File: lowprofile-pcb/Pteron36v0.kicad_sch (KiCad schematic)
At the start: 47 parts, among them J1 AudioJack4, J2 AudioJack4, SW1 SW_PUSH, SW10 SW_PUSH, SW12 SW_PUSH, SW13 SW_PUSH, SW14 SW_PUSH, SW15 SW_PUSH, SW17 SW_PUSH, SW18 SW_PUSH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

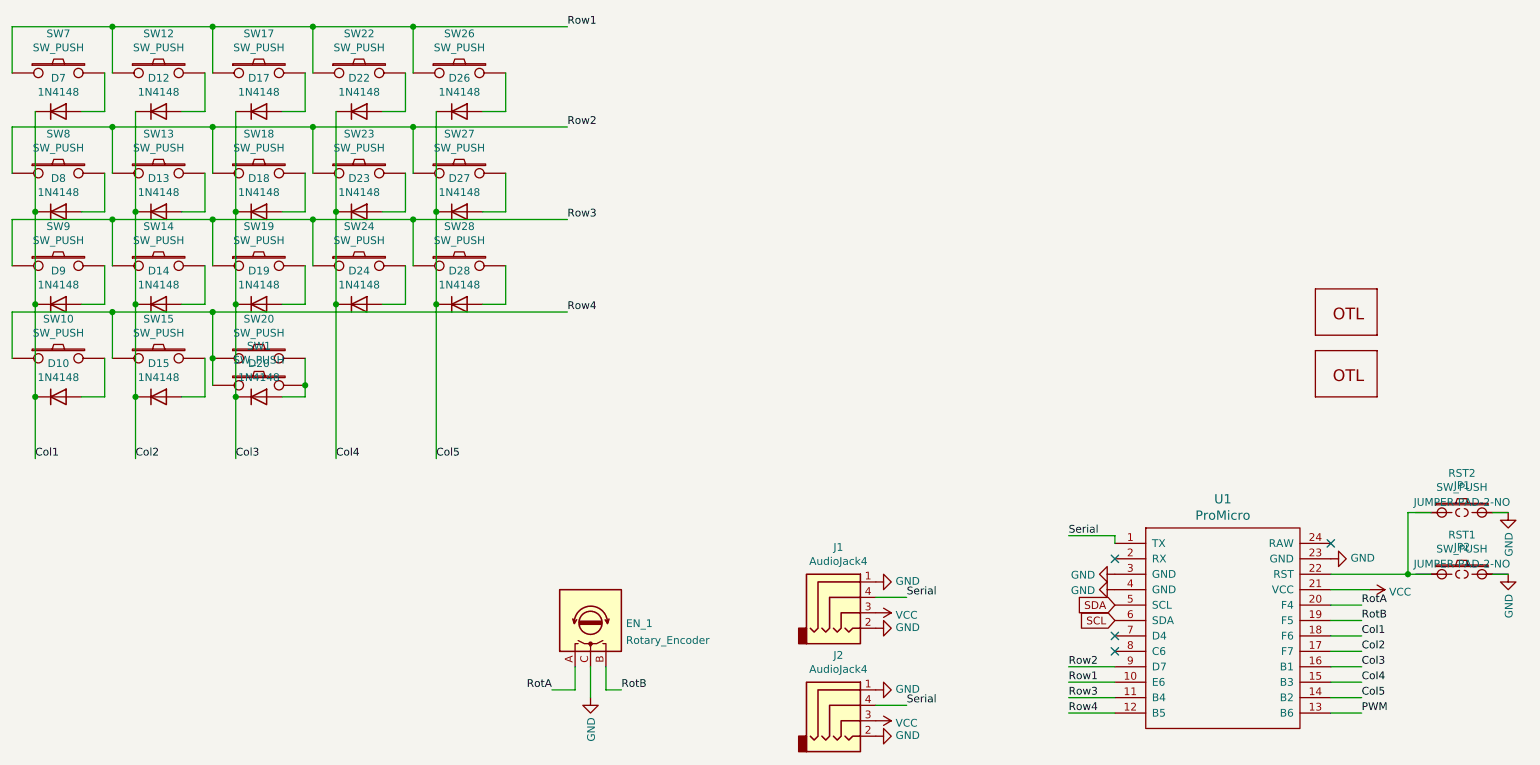
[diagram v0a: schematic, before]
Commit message: add 4-th key in thumb for removable config
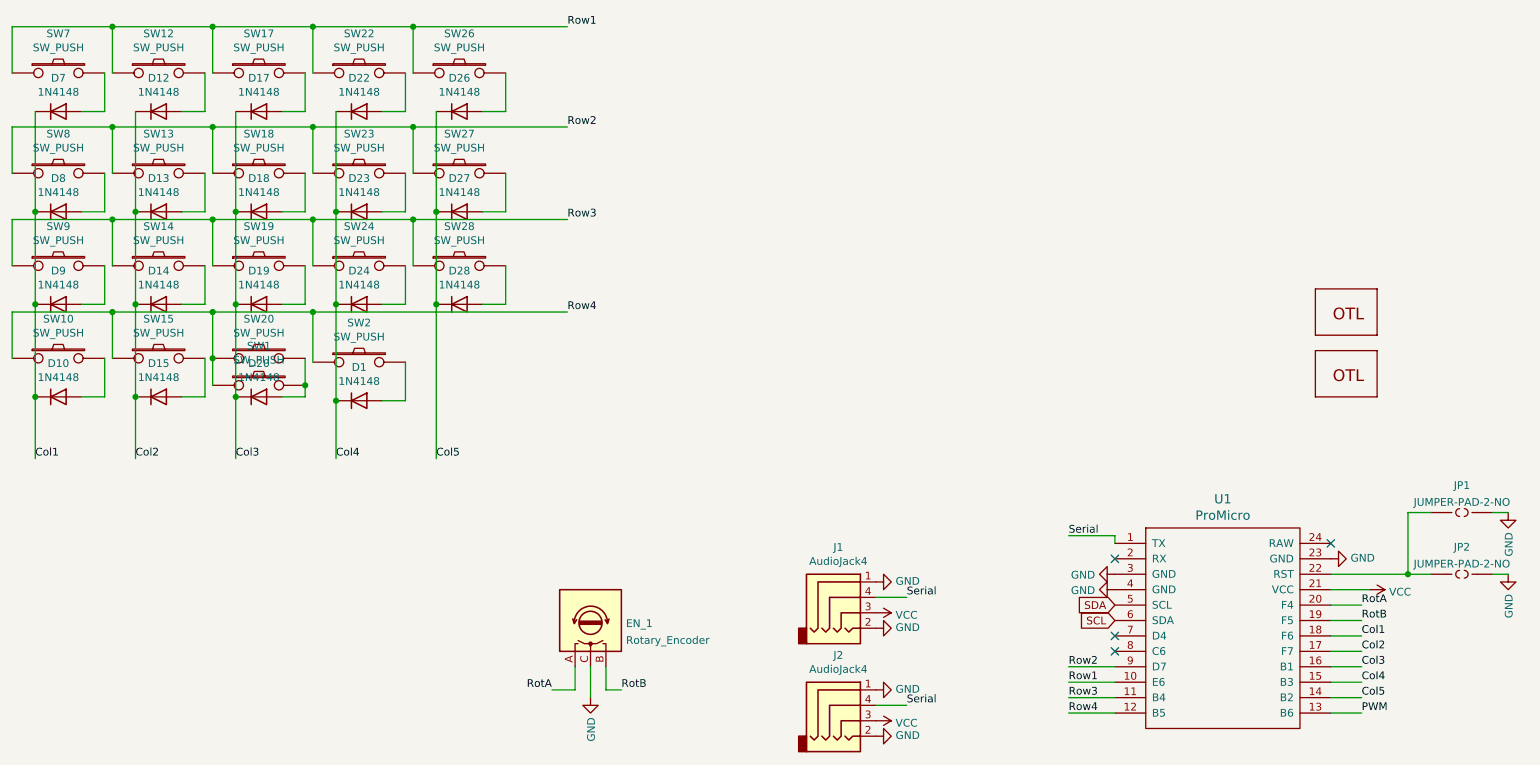
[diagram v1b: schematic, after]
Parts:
- removed RST1, RST2: SW_PUSH, acheron_Hardware:smdPushBtn, symbol keyboard_parts:SW_PUSH
- added D1: 1N4148, Keebio-Parts:Diode-dual, symbol Diode:1N4148
- added SW2: SW_PUSH, keyswitches:PG1350_reversible, symbol keyboard_parts:SW_PUSH
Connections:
- net Col4: now also D1.1 (K)
- net Row4: now also SW2.1
- new net: D1.2 (A), SW2.2
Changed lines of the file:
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@@
   (junction (at 81.28 46.99) (diameter 1.016) (color 0 0 0 0))
   (junction (at 81.28 62.23) (diameter 1.016) (color 0 0 0 0))
+  (junction (at 81.28 77.47) (diameter 1.016) (color 0 0 0 0))
   (junction (at 85.09 60.96) (diameter 1.016) (color 0 0 0 0))
   (junction (at 85.09 76.2) (diameter 1.016) (color 0 0 0 0))
+  (junction (at 85.09 92.075) (diameter 1.016) (color 0 0 0 0))
   (junction (at 97.79 30.48) (diameter 1.016) (color 0 0 0 0))
   (junction (at 97.79 46.99) (diameter 1.016) (color 0 0 0 0))
@@
     (stroke (width 0) (type solid) (color 0 0 0 0))
   )
-  (wire (pts (xy 64.77 77.47) (xy 123.19 77.47))
+  (wire (pts (xy 64.77 77.47) (xy 81.28 77.47))
     (stroke (width 0) (type solid) (color 0 0 0 0))
   )
@@
     (stroke (width 0) (type solid) (color 0 0 0 0))
   )
+  (wire (pts (xy 81.28 77.47) (xy 81.28 85.725))
+    (stroke (width 0) (type solid) (color 0 0 0 0))
+  )
+  (wire (pts (xy 81.28 77.47) (xy 123.19 77.47))
+    (stroke (width 0) (type solid) (color 0 0 0 0))
+  )
   (wire (pts (xy 85.09 60.96) (xy 85.09 44.45))
     (stroke (width 0) (type solid) (color 0 0 0 0))
@@
     (stroke (width 0) (type solid) (color 0 0 0 0))
   )
-  (wire (pts (xy 85.09 76.2) (xy 85.09 101.6))
+  (wire (pts (xy 85.09 76.2) (xy 85.09 92.075))
+    (stroke (width 0) (type solid) (color 0 0 0 0))
+  )
+  (wire (pts (xy 85.09 92.075) (xy 85.09 101.6))
     (stroke (width 0) (type solid) (color 0 0 0 0))
   )
@@
   )
   (wire (pts (xy 96.52 76.2) (xy 92.71 76.2))
+    (stroke (width 0) (type solid) (color 0 0 0 0))
+  )
+  (wire (pts (xy 96.52 85.725) (xy 96.52 92.075))
+    (stroke (width 0) (type solid) (color 0 0 0 0))
+  )
+  (wire (pts (xy 96.52 92.075) (xy 92.71 92.075))
     (stroke (width 0) (type solid) (color 0 0 0 0))
   )
@@
     (pin "2")
   )
+  (symbol (lib_id "Diode:1N4148") (at 88.9 92.075 0) (unit 1)
+    (in_bom yes) (on_board yes)
+    (property "Reference" "D1" (id 0) (at 88.9 86.5632 0))
+    (property "Value" "1N4148" (id 1) (at 88.9 88.8746 0))
+    (property "Footprint" "Keebio-Parts:Diode-dual" (id 2) (at 88.9 96.52 0)
+      (effects (font (size 1.27 1.27)) hide)
+    )
+    (property "Datasheet" "https://assets.nexperia.com/documents/data-sheet/1N4148_1N4448.pdf" (id 3) (at 88.9 92.075 0)
+      (effects (font (size 1.27 1.27)) hide)
+    )
+    (pin "1")
+    (pin "2")
+  )
   (symbol (lib_id "Diode:1N4148") (at 105.41 44.45 0) (unit 1)
     (in_bom yes) (on_board yes)
@@
     (pin "2")
   )
+  (symbol (lib_id "keyboard_parts:SW_PUSH") (at 88.9 85.725 0) (unit 1)
+    (in_bom yes) (on_board yes)
+    (property "Reference" "SW2" (id 0) (at 88.9 79.248 0))
+    (property "Value" "SW_PUSH" (id 1) (at 88.9 81.5594 0))
+    (property "Footprint" "keyswitches:PG1350_reversible" (id 2) (at 88.9 85.725 0)
+      (effects (font (size 1.524 1.524)) hide)
+    )
+    (property "Datasheet" "" (id 3) (at 88.9 85.725 0)
+      (effects (font (size 1.524 1.524)))
+    )
+    (pin "1")
+    (pin "2")
+  )
   (symbol (lib_id "keyboard_parts:SW_PUSH") (at 105.41 38.1 0) (unit 1)
     (in_bom yes) (on_board yes)
@@
     )
     (property "Datasheet" "" (id 3) (at 105.41 69.85 0)
-      (effects (font (size 1.524 1.524)))
-    )
-    (pin "1")
-    (pin "2")
-  )
-  (symbol (lib_id "keyboard_parts:SW_PUSH") (at 270.51 110.49 0) (unit 1)
-    (in_bom yes) (on_board yes)
-    (property "Reference" "RST2" (id 0) (at 270.51 104.013 0))
-    (property "Value" "SW_PUSH" (id 1) (at 270.51 106.3244 0))
-    (property "Footprint" "acheron_Hardware:smdPushBtn" (id 2) (at 270.51 110.49 0)
-      (effects (font (size 1.524 1.524)) hide)
-    )
-    (property "Datasheet" "" (id 3) (at 270.51 110.49 0)
-      (effects (font (size 1.524 1.524)))
-    )
-    (pin "1")
-    (pin "2")
-  )
-  (symbol (lib_id "keyboard_parts:SW_PUSH") (at 270.51 120.65 0) (unit 1)
-    (in_bom yes) (on_board yes)
-    (property "Reference" "RST1" (id 0) (at 270.51 114.173 0))
-    (property "Value" "SW_PUSH" (id 1) (at 270.51 116.4844 0))
-    (property "Footprint" "acheron_Hardware:smdPushBtn" (id 2) (at 270.51 120.65 0)
-      (effects (font (size 1.524 1.524)) hide)
-    )
-    (property "Datasheet" "" (id 3) (at 270.51 120.65 0)
       (effects (font (size 1.524 1.524)))
     )
@@
       (reference "#PWR0118") (unit 1) (value "GND") (footprint "")
     )
+    (path "/703bd629-2fdb-4790-be4c-4af2160ffc24"
+      (reference "D1") (unit 1) (value "1N4148") (footprint "Keebio-Parts:Diode-dual")
+    )
     (path "/00000000-0000-0000-0000-000060962387"
       (reference "D7") (unit 1) (value "1N4148") (footprint "Keebio-Parts:Diode-dual")
@@
       (reference "J2") (unit 1) (value "AudioJack4") (footprint "Keebio-Parts:TRRS-PJ-320A")
     )
+    (path "/0b76a048-da1d-4d10-82af-9264c0605235"
+      (reference "JP1") (unit 1) (value "JUMPER-PAD-2-NO") (footprint "Jumper:SolderJumper-2_P1.3mm_Open_Pad1.0x1.5mm")
+    )
+    (path "/c097909c-92c1-4c73-bddc-504d7eb669e6"
+      (reference "JP2") (unit 1) (value "JUMPER-PAD-2-NO") (footprint "Jumper:SolderJumper-2_P1.3mm_Open_Pad1.0x1.5mm")
+    )
     (path "/e4d4d865-3cb1-431d-b18c-3cc2928a93c9"
       (reference "LOGO3") (unit 1) (value "LOGO-OTL") (footprint "personal-logo:peacock-medium")
@@
       (reference "LOGO4") (unit 1) (value "LOGO-OTL") (footprint "personal-logo:peacock-medium")
     )
-    (path "/00000000-0000-0000-0000-0000607b81a2"
-      (reference "RST1") (unit 1) (value "SW_PUSH") (footprint "acheron_Hardware:smdPushBtn")
-    )
-    (path "/00000000-0000-0000-0000-0000607e0b2f"
-      (reference "RST2") (unit 1) (value "SW_PUSH") (footprint "acheron_Hardware:smdPushBtn")
-    )
     (path "/402851d8-0ae4-4da3-93c1-370c6cc5e9c2"
       (reference "SW1") (unit 1) (value "SW_PUSH") (footprint "keyswitches:PG1350_reversible")
     )
+    (path "/7cfaa52c-f5a8-40c1-8338-4b4531af7830"
+      (reference "SW2") (unit 1) (value "SW_PUSH") (footprint "keyswitches:PG1350_reversible")
+    )
     (path "/00000000-0000-0000-0000-000060963566"
